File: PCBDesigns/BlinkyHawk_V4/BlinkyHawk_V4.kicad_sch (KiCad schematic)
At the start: 54 parts, among them J3 Conn_01x07_Pin, J4 Battery, J5 Conn_01x01, J6 Conn_01x07_Pin, J7 Conn_01x01, Q1 AO3400A MOSFET, Q2 AO3400A MOSFET, Q3 AO3401A, SW1 SW_Push_DPDT, SW2 XY-TBT5858-W-FL, SW4 SW_SPDT, U1 TPS22914BYFPR, U3 TL431DBZ, U4 TPS22914BYFPR, U5 PAM8904JER, U9 TPS613222ADBV

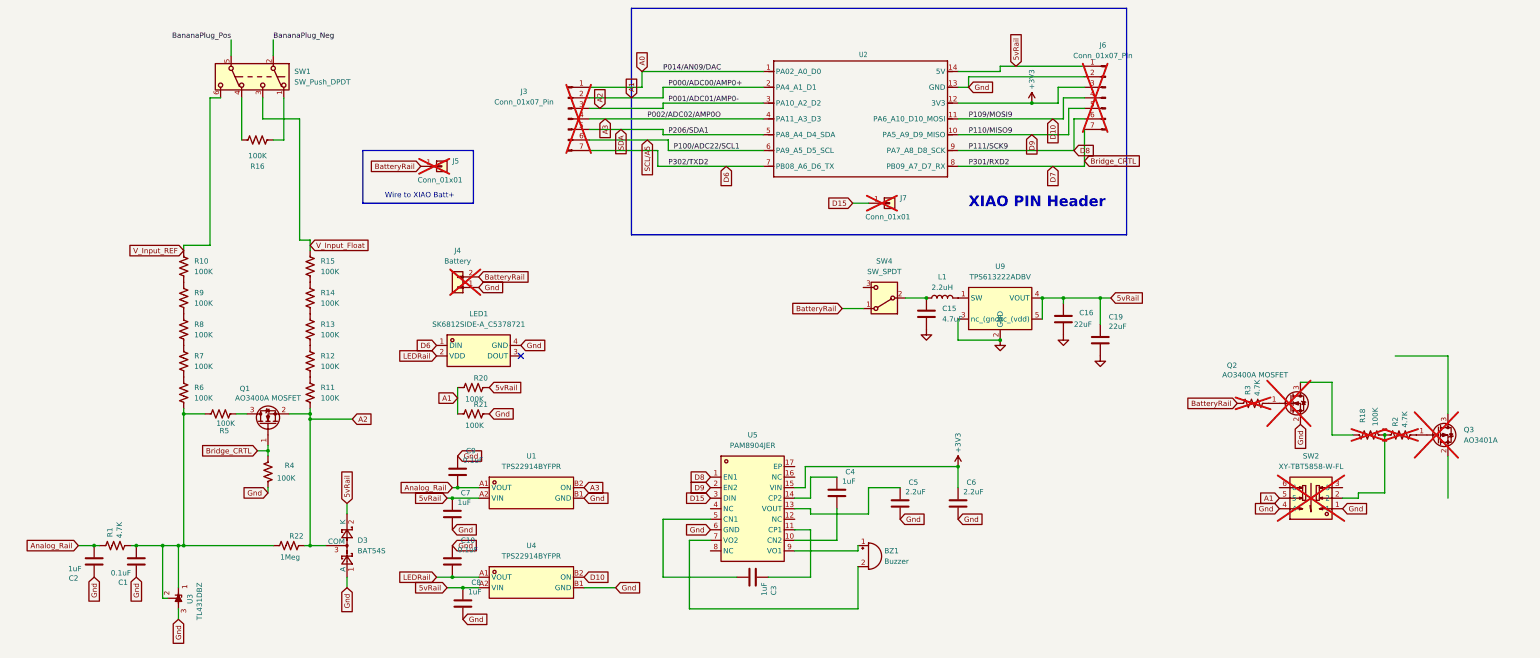
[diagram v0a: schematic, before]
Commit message: Created a battery runtime calc, tuned units.
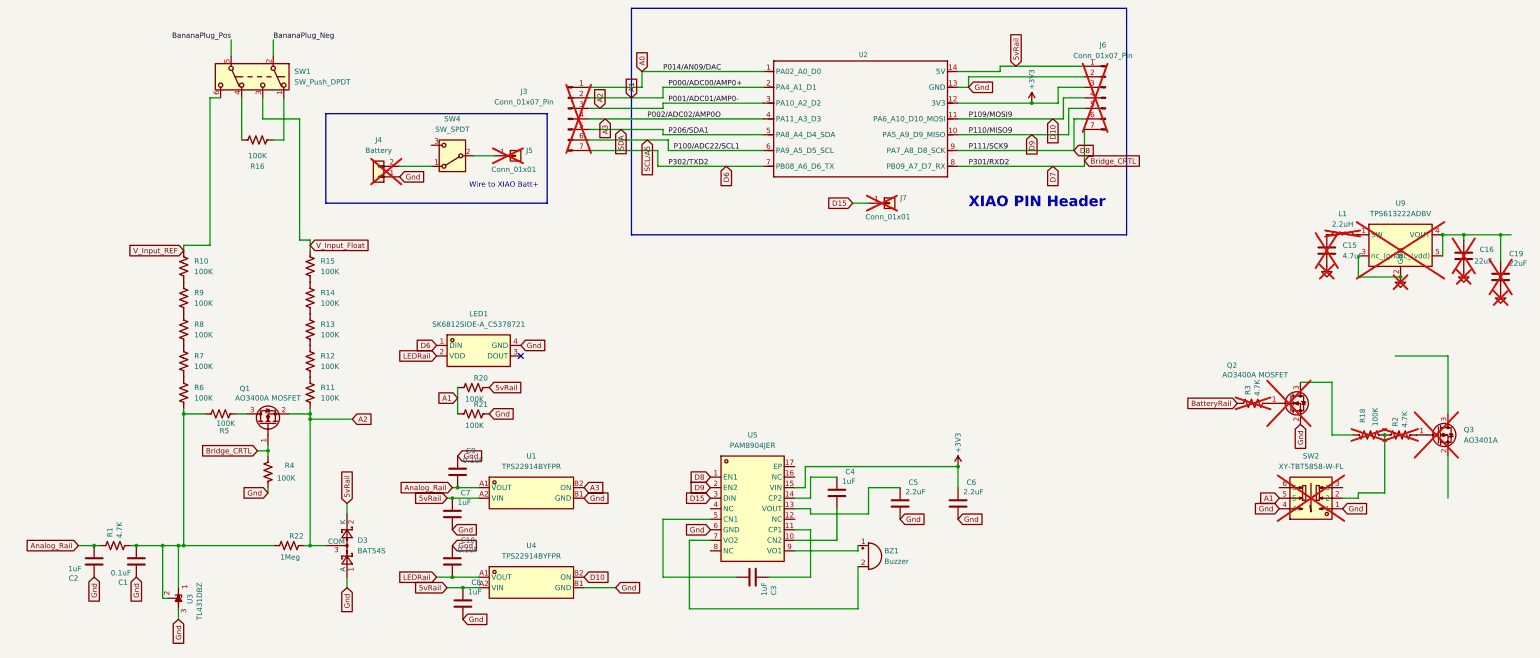
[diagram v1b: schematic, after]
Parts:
- C15, C16, C19, L1, U9: now not fitted
- J4: footprint Connector_PinHeader_1.27mm:PinHeader_1x02_P1.27mm_Vertical -> Connector_Molex:Molex_PicoBlade_53398-0271_1x02-1MP_P1.25mm_Vertical
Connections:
- net 5vRail: no longer C16.1, C19.1, U9.4 (VOUT), U9.5 (nc_(vdd))
- net BatteryRail: no longer J4.2 (Pin_2), J5.1 (Pin_1), SW4.1 (A)
- net at C15.1, L1.1: no longer SW4.2 (B)
- new net: C16.1, C19.1, U9.4 (VOUT), U9.5 (nc_(vdd))
- new net: J4.2 (Pin_2), SW4.1 (A)
- new net: J5.1 (Pin_1), SW4.2 (B)
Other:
- moved on the sheet: J4, J5, SW4
